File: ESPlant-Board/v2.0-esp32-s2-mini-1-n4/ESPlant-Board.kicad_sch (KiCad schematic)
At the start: 30 parts, among them J1 Conn_01x05, U1 ESP32-S2-MINI-1-N4, U3 Reset, U4 Boot, U5 Temp/Humid-Sensor, U6 Light sensor, U7 AMS1117-3_3, U8 MK-12C02-G025

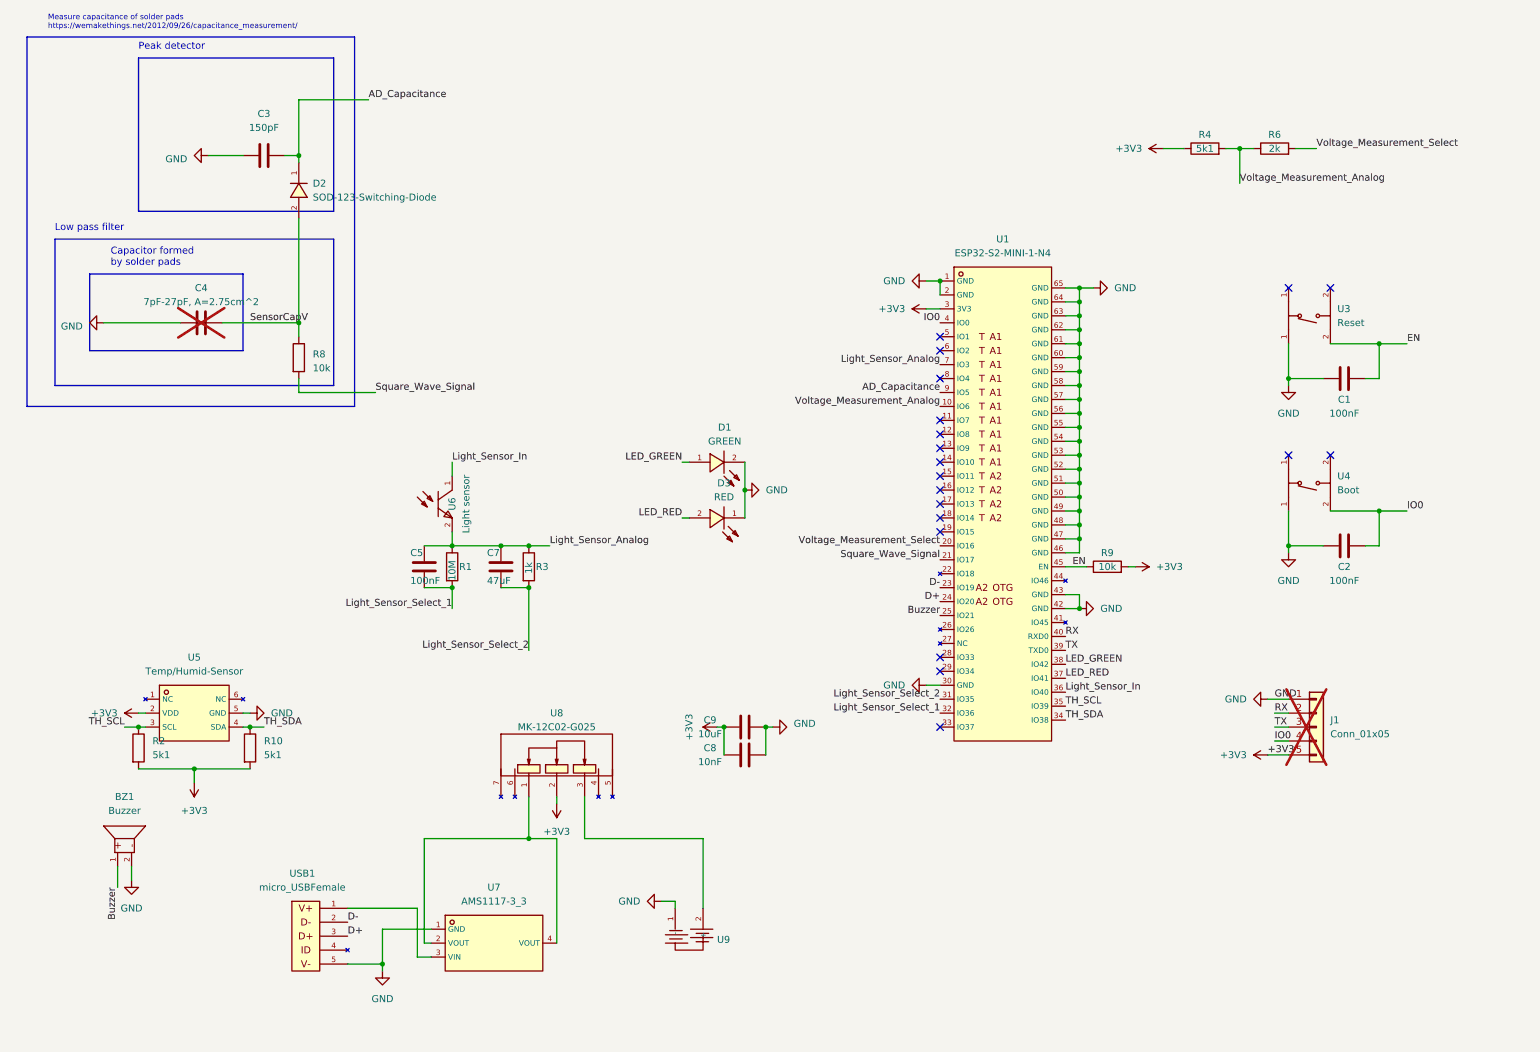
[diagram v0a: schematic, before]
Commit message: Case: Add v2 case with improved folder structure
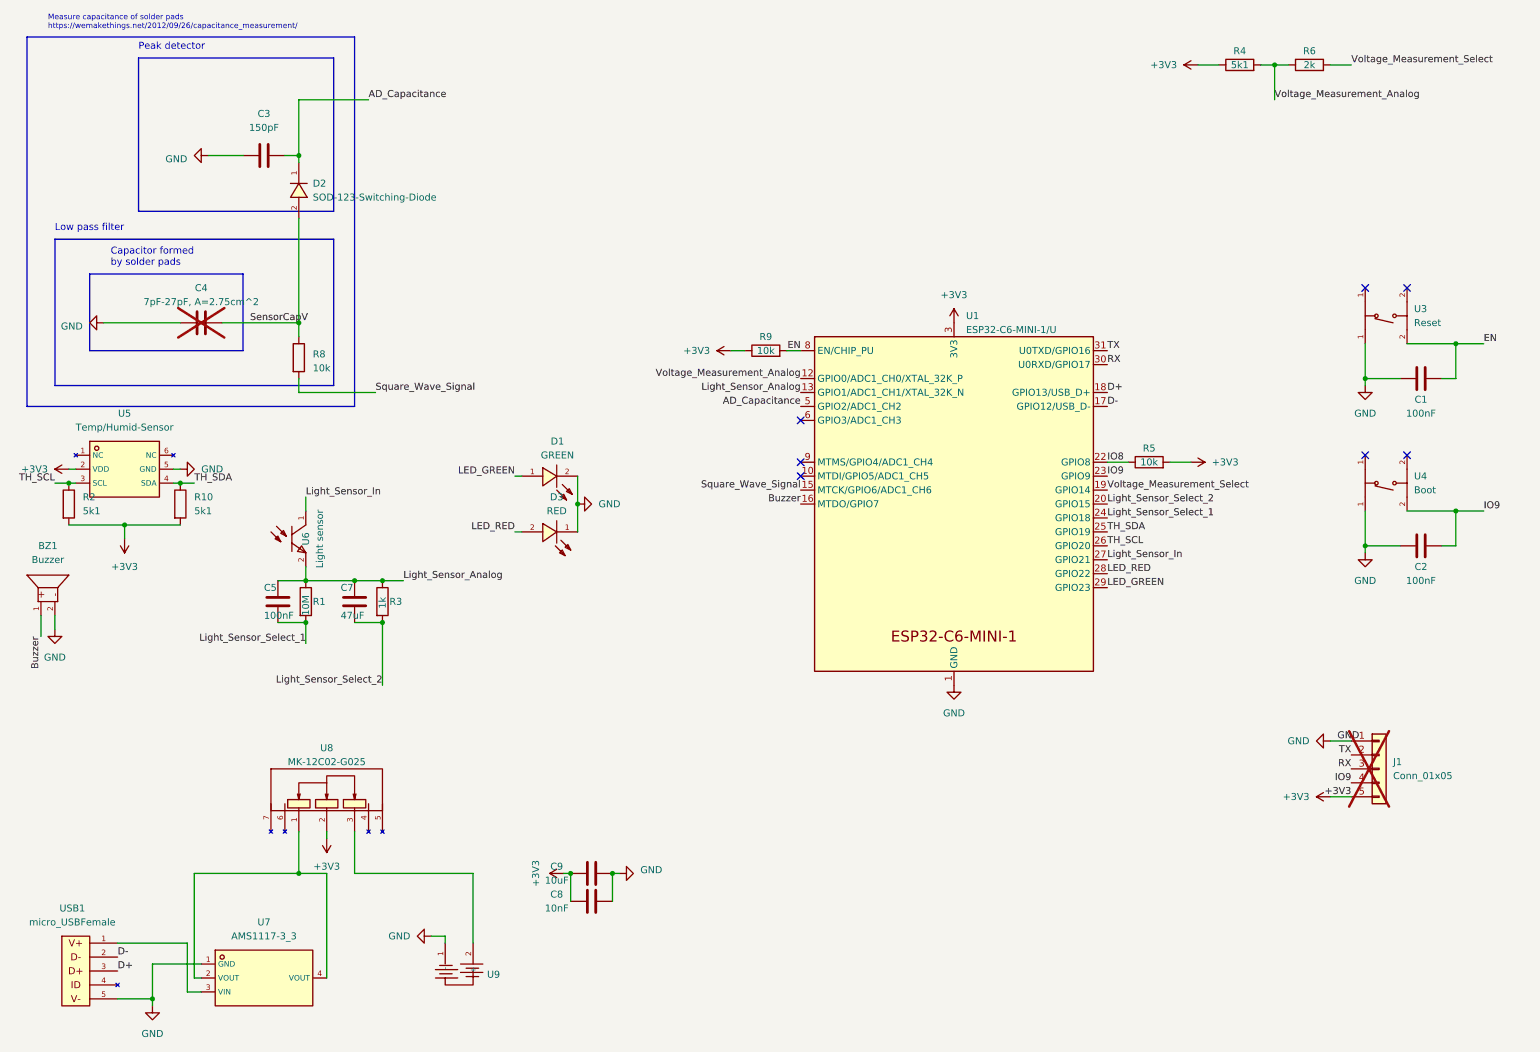
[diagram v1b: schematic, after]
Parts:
- removed U1: ESP32-S2-MINI-1-N4, CustomFootprints:WIFI-SMD_ESP32-MINI-1-N4, symbol Custom_Parts:ESP32-S2-MINI-1-N4
- added R5: 10k, Resistor_SMD:R_0402_1005Metric, symbol Device:R
- added U1: ESP32-C6-MINI-1/U, Espressif:ESP32-C6-MINI-1, symbol Espressif:ESP32-C6-MINI-1/U
- C4, J1, U9: LCSC (none) -> /; MPN (none) -> /
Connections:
- net IO0 is gone; now on net IO9: C2.2, J1.4 (Pin_4), U4.2 (D)
- net +3V3: now also R9.1, R5.2, U1.3 (3V3); no longer R9.2
- net AD_Capacitance: now also U1.5 (GPIO2/ADC1_CH2)
- net Buzzer: now also U1.16 (MTDO/GPIO7)
- net D+: now also U1.18 (GPIO13/USB_D+)
- net D-: now also U1.17 (GPIO12/USB_D-)
- net EN: now also R9.2, U1.8 (EN/CHIP_PU); no longer R9.1
- net GND: now also U1.1 (GND), U1.11 (GND), U1.14 (GND), U1.2 (GND), U1.36 (GND), U1.37 (GND), U1.38 (GND), U1.39 (GND), U1.40 (GND), U1.41 (GND), U1.42 (GND), U1.43 (GND), U1.44 (GND), U1.45 (GND), U1.46 (GND), U1.47 (GND), U1.48 (GND), U1.49 (GND), U1.50 (GND), U1.51 (GND), U1.52 (GND), U1.53 (GND)
- net LED_GREEN: now also U1.29 (GPIO23)
- net LED_RED: now also U1.28 (GPIO22)
- net Light_Sensor_Analog: now also U1.13 (GPIO1/ADC1_CH1/XTAL_32K_N)
- net Light_Sensor_In: now also U1.27 (GPIO21)
- net Light_Sensor_Select_1: now also U1.24 (GPIO18)
- net Light_Sensor_Select_2: now also U1.20 (GPIO15)
- net RX: now also J1.3 (Pin_3), U1.30 (U0RXD/GPIO17); no longer J1.2 (Pin_2)
- net Square_Wave_Signal: now also U1.15 (MTCK/GPIO6/ADC1_CH6)
- net TH_SCL: now also U1.26 (GPIO20)
- net TH_SDA: now also U1.25 (GPIO19)
- net TX: now also J1.2 (Pin_2), U1.31 (U0TXD/GPIO16); no longer J1.3 (Pin_3)
- net Voltage_Measurement_Analog: now also U1.12 (GPIO0/ADC1_CH0/XTAL_32K_P)
- net Voltage_Measurement_Select: now also U1.19 (GPIO14)
- net IO9: now reaches U4.2 (D)
- net IO9: now also U1.23 (GPIO9)
- new net IO8: R5.1, U1.22 (GPIO8)
- no-connect marks 19 -> 7
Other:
- moved on the sheet: BZ1, C1, C2, C5, C7, C8, C9, D1, D3, R1, R10, R2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
